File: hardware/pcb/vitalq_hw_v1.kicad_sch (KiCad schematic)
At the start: 2 parts

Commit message: Rebuild the hw_v1 board around the reduced part list.
Replace the stub hierarchy and import-grid PCB with an explicit
seven-sheet schematic and a 52 x 40 mm two-sided wearable placement.
AS7341 stays on a 1.8 V TPS7A2018, with one PCA9306 for its I2C bus.

Co-authored-by: Riyu-D1 <Riyu-D1@users.noreply.github.com>
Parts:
- removed PFLG1, PFLG2: PWR_FLAG, symbol power:PWR_FLAG
- added C1, C2: 4.7u, Capacitor_SMD:C_0402_1005Metric, symbol vitalq:C
- added C3, C4, C5, C6: 1u, Capacitor_SMD:C_0402_1005Metric, symbol vitalq:C
- added H1, H2: M2, MountingHole:MountingHole_2.2mm_M2, symbol vitalq:MountingHole
- added J1: USB-C, Connector_USB:USB_C_Receptacle_HRO_TYPE-C-31-M-12, symbol vitalq:USB_C_Receptacle_USB2.0_16P
- added J2: LiPo, Connector_JST:JST_PH_S2B-PH-SM4-TB_1x02-1MP_P2.00mm_Horizontal, symbol vitalq:Conn_01x02_Pin
- added R1, R2: 5.1k, Resistor_SMD:R_0402_1005Metric, symbol vitalq:R
- added R3: 10k, Resistor_SMD:R_0402_1005Metric, symbol vitalq:R
- added U2: MCP73831T-2ACI/OT, Package_TO_SOT_SMD:SOT-23-5, symbol vitalq:MCP73831-2-OT
- added U3: XC6206P332MR-G, Package_TO_SOT_SMD:SOT-23-3, symbol vitalq:XC6206PxxxMR
- added U4: TPS7A2018PDBVR, Package_TO_SOT_SMD:SOT-23-5, symbol vitalq:TPS7A2018PDBVR
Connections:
- net GND: now also C1.2, C2.2, C3.2, C4.2, C5.2, C6.2, J1.A1 (GND), J1.A12 (GND), J1.B1 (GND), J1.B12 (GND), J1.S1 (SHIELD), J2.2 (Pin_2), R1.2, R2.2, R3.2, U2.2 (V_{SS}), U3.1 (GND), U4.2 (GND)
- net VBUS: now also C1.1, J1.A4 (VBUS), J1.A9 (VBUS), J1.B4 (VBUS), J1.B9 (VBUS), U2.4 (V_{DD})
- new net +1V8: C6.1, U4.5 (OUT)
- new net +3V3: C4.1, C5.1, U3.2 (VO), U4.1 (IN), U4.3 (EN)
- new net CHG_PROG: R3.1, U2.5 (PROG)
- new net USB_CC1: J1.A5 (CC1), R1.1
- new net USB_CC2: J1.B5 (CC2), R2.1
- new net USB_DM: J1.A7 (D-), J1.B7 (D-)
- new net USB_DP: J1.A6 (D+), J1.B6 (D+)
- new net VBAT: C2.1, C3.1, J2.1 (Pin_1), U2.3 (V_{BAT}), U3.3 (VI)
- no-connect marks 0 -> 3
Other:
- removed sheet contact
- removed sheet i2c_sensors
- removed sheet mcu
- removed sheet power
- removed sheet spi_afes
- removed sheet usb
- added sheet AD5940 EDA (ad5940.kicad_sch)
- added sheet ADS1292R ECG (ads1292.kicad_sch)
- added sheet AFE4900 PPG (afe4900.kicad_sch)
- added sheet I2C and IMU (i2c.kicad_sch)
- added sheet MCU and FSR (mcu.kicad_sch)
- added sheet USB-UART (usb.kicad_sch)
- note added: "Decoupling"
- note added: "Load sits on VBAT. USB charges the cell and powers the UART. The board does not run from USB with the cell missing."
- note added: "Other sheets"
- note added: "Power and charging"
- note added: "R3 = 10k sets MCP73831 to 100 mA. STAT is open. No charge LED. H1 and H2 are M2 holes."
- note added: "Sheets below contain the parts. They are not empty stubs."
- note added: "TPS7A2018 (not 3.3 V): AS7341 VDD is 1.7-2.0 V. Every other IC runs at 3.3 V."
- note added: "U4 is fed from U3. EN is tied to IN. No separate 1.8 V XC6206."
- note added: "USB-C, LiPo charger, 3.3 V rail, 1.8 V rail"
- company: (none) -> VitalQ
- title: VitalQ hw_v1 research prototype — wiring only, not placed -> Power and charging

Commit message: Use official CAD and shrink the hw_v1 board to 37x30 mm.
Replace the hand-drawn AFE4900, AD5940, ADS1292R, AS7341, MLX90632,
TMP117, LSM6DSV80X, and MCP73831 symbols and footprints with the
SnapMagic and Ultra Librarian libraries. ADS1292R is now the QFN-32
ADS1292RIRSMT, and MLX90632SLD-DCB-100-SP moves SDA/SCL onto the
existing 1.8 V bus. Pin headers and mounting holes are flat solder
pads. The unrouted 4-layer placement keeps the antenna on the left
edge and the skin sensors together on the bottom.

Co-authored-by: Riyu-D1 <Riyu-D1@users.noreply.github.com>
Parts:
- removed H1, H2: M2, MountingHole:MountingHole_2.2mm_M2, symbol vitalq:MountingHole
- removed U2: MCP73831T-2ACI/OT, Package_TO_SOT_SMD:SOT-23-5, symbol vitalq:MCP73831-2-OT
- added U2: MCP73831T-2ACI/OT, snap:SOT95P280X145-5N, symbol vitalq:MCP73831T-2ACI_OT
- J2: value LiPo -> LiPo pads; footprint Connector_JST:JST_PH_S2B-PH-SM4-TB_1x02-1MP_P2.00mm_Horizontal -> vitalq:Pads_LiPo
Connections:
- net CHG_PROG: now also U2.5 (PROG)
- net GND: now also U2.2 (VSS)
- net VBAT: now also U2.3 (VBAT)
- net VBUS: now also U2.4 (VDD)
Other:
- note added: "J2 is two flat solder pads (BAT+ BAT-), not a header. No power switch."

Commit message: Pack the hw_v1 board to 36.2 x 28 mm and correct the 3D models.
The LSM6 body is a 3.0 x 2.5 x 0.83 mm box in KiCad VRML units, and the other vendor models are rotated so they stand on their lands. Skin sensors sit in one bottom cluster with the electrode pads around them, bypass parts are packed next to their ICs outside the antenna keep-out, and the schematic frames clear the title block.

Co-authored-by: Riyu-D1 <Riyu-D1@users.noreply.github.com>
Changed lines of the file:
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@@
 		(instances
 			(project "vitalq_hw_v1"
-				(path "/3a03f3a2-f664-49ab-a6e3-0e34faafa582"
+				(path "/6fcf6b13-4a8e-4f25-a8b9-d34cb547168d"
 					(reference "J1")
 					(unit 1)
@@
 		(instances
 			(project "vitalq_hw_v1"
-				(path "/3a03f3a2-f664-49ab-a6e3-0e34faafa582"
+				(path "/6fcf6b13-4a8e-4f25-a8b9-d34cb547168d"
 					(reference "#PWR001")
 					(unit 1)
@@
 		(instances
 			(project "vitalq_hw_v1"
-				(path "/3a03f3a2-f664-49ab-a6e3-0e34faafa582"
+				(path "/6fcf6b13-4a8e-4f25-a8b9-d34cb547168d"
 					(reference "#PWR002")
 					(unit 1)
@@
 		(instances
 			(project "vitalq_hw_v1"
-				(path "/3a03f3a2-f664-49ab-a6e3-0e34faafa582"
+				(path "/6fcf6b13-4a8e-4f25-a8b9-d34cb547168d"
 					(reference "R1")
 					(unit 1)
@@
 		(instances
 			(project "vitalq_hw_v1"
-				(path "/3a03f3a2-f664-49ab-a6e3-0e34faafa582"
+				(path "/6fcf6b13-4a8e-4f25-a8b9-d34cb547168d"
 					(reference "#PWR003")
 					(unit 1)
@@
 		(instances
 			(project "vitalq_hw_v1"
-				(path "/3a03f3a2-f664-49ab-a6e3-0e34faafa582"
+				(path "/6fcf6b13-4a8e-4f25-a8b9-d34cb547168d"
 					(reference "R2")
 					(unit 1)
@@
 		(instances
 			(project "vitalq_hw_v1"
-				(path "/3a03f3a2-f664-49ab-a6e3-0e34faafa582"
+				(path "/6fcf6b13-4a8e-4f25-a8b9-d34cb547168d"
 					(reference "#PWR004")
 					(unit 1)
@@
 		(instances
 			(project "vitalq_hw_v1"
-				(path "/3a03f3a2-f664-49ab-a6e3-0e34faafa582"
+				(path "/6fcf6b13-4a8e-4f25-a8b9-d34cb547168d"
 					(reference "U2")
 					(unit 1)
@@
 		(instances
 			(project "vitalq_hw_v1"
-				(path "/3a03f3a2-f664-49ab-a6e3-0e34faafa582"
+				(path "/6fcf6b13-4a8e-4f25-a8b9-d34cb547168d"
 					(reference "R3")
 					(unit 1)
@@
 		(instances
 			(project "vitalq_hw_v1"
-				(path "/3a03f3a2-f664-49ab-a6e3-0e34faafa582"
+				(path "/6fcf6b13-4a8e-4f25-a8b9-d34cb547168d"
 					(reference "#PWR005")
 					(unit 1)
@@
 		(instances
 			(project "vitalq_hw_v1"
-				(path "/3a03f3a2-f664-49ab-a6e3-0e34faafa582"
+				(path "/6fcf6b13-4a8e-4f25-a8b9-d34cb547168d"
 					(reference "U3")
 					(unit 1)
@@
 		(instances
 			(project "vitalq_hw_v1"
-				(path "/3a03f3a2-f664-49ab-a6e3-0e34faafa582"
+				(path "/6fcf6b13-4a8e-4f25-a8b9-d34cb547168d"
 					(reference "#PWR006")
 					(unit 1)
@@
 		(instances
 			(project "vitalq_hw_v1"
-				(path "/3a03f3a2-f664-49ab-a6e3-0e34faafa582"
+				(path "/6fcf6b13-4a8e-4f25-a8b9-d34cb547168d"
 					(reference "U4")
 					(unit 1)
@@
 		(instances
 			(project "vitalq_hw_v1"
-				(path "/3a03f3a2-f664-49ab-a6e3-0e34faafa582"
+				(path "/6fcf6b13-4a8e-4f25-a8b9-d34cb547168d"
 					(reference "#PWR007")
 					(unit 1)
@@
 		(instances
 			(project "vitalq_hw_v1"
-				(path "/3a03f3a2-f664-49ab-a6e3-0e34faafa582"
+				(path "/6fcf6b13-4a8e-4f25-a8b9-d34cb547168d"
 					(reference "J2")
 					(unit 1)
@@
 		(instances
 			(project "vitalq_hw_v1"
-				(path "/3a03f3a2-f664-49ab-a6e3-0e34faafa582"
+				(path "/6fcf6b13-4a8e-4f25-a8b9-d34cb547168d"
 					(reference "C1")
 					(unit 1)
@@
 		(instances
 			(project "vitalq_hw_v1"
-				(path "/3a03f3a2-f664-49ab-a6e3-0e34faafa582"
+				(path "/6fcf6b13-4a8e-4f25-a8b9-d34cb547168d"
 					(reference "#PWR008")
 					(unit 1)
@@
 		(instances
 			(project "vitalq_hw_v1"
-				(path "/3a03f3a2-f664-49ab-a6e3-0e34faafa582"
+				(path "/6fcf6b13-4a8e-4f25-a8b9-d34cb547168d"
 					(reference "#PWR009")
 					(unit 1)
@@
 		(instances
 			(project "vitalq_hw_v1"
-				(path "/3a03f3a2-f664-49ab-a6e3-0e34faafa582"
+				(path "/6fcf6b13-4a8e-4f25-a8b9-d34cb547168d"
 					(reference "C2")
 					(unit 1)
@@
 		(instances
 			(project "vitalq_hw_v1"
-				(path "/3a03f3a2-f664-49ab-a6e3-0e34faafa582"
+				(path "/6fcf6b13-4a8e-4f25-a8b9-d34cb547168d"
 					(reference "#PWR010")
 					(unit 1)
@@
 		(instances
 			(project "vitalq_hw_v1"
-				(path "/3a03f3a2-f664-49ab-a6e3-0e34faafa582"
+				(path "/6fcf6b13-4a8e-4f25-a8b9-d34cb547168d"
 					(reference "C3")
 					(unit 1)
@@
 		(instances
 			(project "vitalq_hw_v1"
-				(path "/3a03f3a2-f664-49ab-a6e3-0e34faafa582"
+				(path "/6fcf6b13-4a8e-4f25-a8b9-d34cb547168d"
 					(reference "#PWR011")
 					(unit 1)
@@
 		(instances
 			(project "vitalq_hw_v1"
-				(path "/3a03f3a2-f664-49ab-a6e3-0e34faafa582"
+				(path "/6fcf6b13-4a8e-4f25-a8b9-d34cb547168d"
 					(reference "C4")
 					(unit 1)
@@
 		(instances
 			(project "vitalq_hw_v1"
-				(path "/3a03f3a2-f664-49ab-a6e3-0e34faafa582"
+				(path "/6fcf6b13-4a8e-4f25-a8b9-d34cb547168d"
 					(reference "#PWR012")
 					(unit 1)
@@
 		(instances
 			(project "vitalq_hw_v1"
-				(path "/3a03f3a2-f664-49ab-a6e3-0e34faafa582"
+				(path "/6fcf6b13-4a8e-4f25-a8b9-d34cb547168d"
 					(reference "#PWR013")
 					(unit 1)
@@
 		(instances
 			(project "vitalq_hw_v1"
-				(path "/3a03f3a2-f664-49ab-a6e3-0e34faafa582"
+				(path "/6fcf6b13-4a8e-4f25-a8b9-d34cb547168d"
 					(reference "C5")
 					(unit 1)
@@
 		(instances
 			(project "vitalq_hw_v1"
-				(path "/3a03f3a2-f664-49ab-a6e3-0e34faafa582"
+				(path "/6fcf6b13-4a8e-4f25-a8b9-d34cb547168d"
 					(reference "#PWR014")
 					(unit 1)
@@
 		(instances
 			(project "vitalq_hw_v1"
-				(path "/3a03f3a2-f664-49ab-a6e3-0e34faafa582"
+				(path "/6fcf6b13-4a8e-4f25-a8b9-d34cb547168d"
 					(reference "#PWR015")
 					(unit 1)
@@
 		(instances
 			(project "vitalq_hw_v1"
-				(path "/3a03f3a2-f664-49ab-a6e3-0e34faafa582"
+				(path "/6fcf6b13-4a8e-4f25-a8b9-d34cb547168d"
 					(reference "C6")
 					(unit 1)
@@
 		(instances
 			(project "vitalq_hw_v1"
-				(path "/3a03f3a2-f664-49ab-a6e3-0e34faafa582"
+				(path "/6fcf6b13-4a8e-4f25-a8b9-d34cb547168d"
 					(reference "#PWR016")
 					(unit 1)
@@
 		(instances
 			(project "vitalq_hw_v1"
-				(path "/3a03f3a2-f664-49ab-a6e3-0e34faafa582"
+				(path "/6fcf6b13-4a8e-4f25-a8b9-d34cb547168d"
 					(reference "#PWR017")
 					(unit 1)
@@
 		(instances
 			(project "vitalq_hw_v1"
-				(path "/3a03f3a2-f664-49ab-a6e3-0e34faafa582"
+				(path "/6fcf6b13-4a8e-4f25-a8b9-d34cb547168d"
 					(reference "#PWR018")
 					(unit 1)
@@
 		(instances
 			(project "vitalq_hw_v1"
-				(path "/3a03f3a2-f664-49ab-a6e3-0e34faafa582"
+				(path "/6fcf6b13-4a8e-4f25-a8b9-d34cb547168d"
 					(reference "#FLG019")
 					(unit 1)
@@
 		(instances
 			(project "vitalq_hw_v1"
-				(path "/3a03f3a2-f664-49ab-a6e3-0e34faafa582"
+				(path "/6fcf6b13-4a8e-4f25-a8b9-d34cb547168d"
 					(reference "#PWR020")
 					(unit 1)
@@
 		(instances
 			(project "vitalq_hw_v1"
-				(path "/3a03f3a2-f664-49ab-a6e3-0e34faafa582"
+				(path "/6fcf6b13-4a8e-4f25-a8b9-d34cb547168d"
 					(reference "#FLG021")
 					(unit 1)
@@
 	)
 	(rectangle
-		(start 12.0 20.0)
-		(end 408.0 200.0)
+		(start 12.0 40.0)
+		(end 406.0 200.0)
 		(stroke (width 0.4) (type dash))
 		(fill (type none))
@@
 		(instances
 			(project "vitalq_hw_v1"
-				(path "/3a03f3a2-f664-49ab-a6e3-0e34faafa582"
+				(path "/6fcf6b13-4a8e-4f25-a8b9-d34cb547168d"
 					(page "2")
 				)
@@
 		(instances
 			(project "vitalq_hw_v1"
-				(path "/3a03f3a2-f664-49ab-a6e3-0e34faafa582"
+				(path "/6fcf6b13-4a8e-4f25-a8b9-d34cb547168d"
 					(page "3")
 				)
@@
 		(instances
 			(project "vitalq_hw_v1"
-				(path "/3a03f3a2-f664-49ab-a6e3-0e34faafa582"
+				(path "/6fcf6b13-4a8e-4f25-a8b9-d34cb547168d"
 					(page "4")
 				)
@@
 		(instances
 			(project "vitalq_hw_v1"
-				(path "/3a03f3a2-f664-49ab-a6e3-0e34faafa582"
+				(path "/6fcf6b13-4a8e-4f25-a8b9-d34cb547168d"
 					(page "5")
 				)
@@
 		(instances
 			(project "vitalq_hw_v1"
-				(path "/3a03f3a2-f664-49ab-a6e3-0e34faafa582"
+				(path "/6fcf6b13-4a8e-4f25-a8b9-d34cb547168d"
 					(page "6")
 				)
@@
 		(instances
 			(project "vitalq_hw_v1"
-				(path "/3a03f3a2-f664-49ab-a6e3-0e34faafa582"
+				(path "/6fcf6b13-4a8e-4f25-a8b9-d34cb547168d"
 					(page "7")
 				)

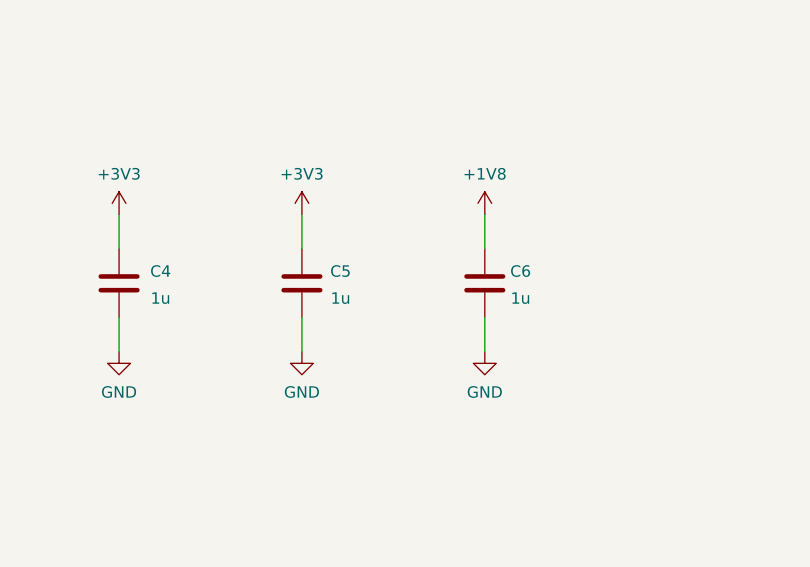
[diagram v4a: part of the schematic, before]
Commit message: Seat the QFN models and drop passives the datasheets do not require.
The ADS1292R STEP is already Z-up, so the extra X rotation stood the
4x4x1 mm body on edge. Remove TP1, TP2, C5, C12, C17, C31 and R4, add
the 1 uF AVDD bulk capacitor, and shorten the outline to 36.2 x 27.8 mm.

Co-authored-by: Riyu-D1 <Riyu-D1@users.noreply.github.com>
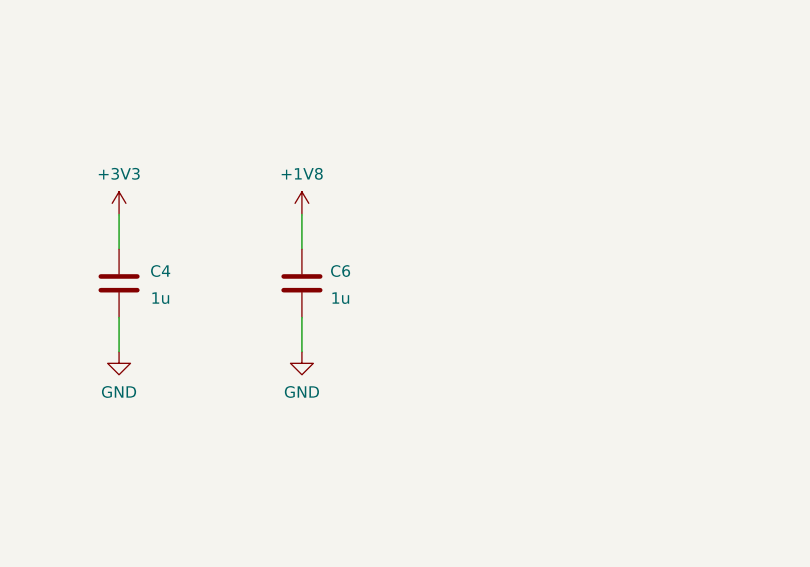
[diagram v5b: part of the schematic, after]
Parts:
- removed C5: 1u, Capacitor_SMD:C_0402_1005Metric, symbol vitalq:C

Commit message: Add the chest-board sensors and replace the 3.3 V LDO with a TPS63802.
The unrouted 40 x 34 mm board keeps every previous part except the off-board PPG pads, which the SFH 7072 replaces. Respiration, a second ECG lead, electrode protection, EDA, fuel gauge, flash, and the I/O expander are in the schematic.

Co-authored-by: Riyu-D1 <Riyu-D1@users.noreply.github.com>
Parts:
- removed U3: XC6206P332MR-G, Package_TO_SOT_SMD:SOT-23-3, symbol vitalq:XC6206PxxxMR
- added C44: 10u, Capacitor_SMD:C_0603_1608Metric, symbol vitalq:C
- added C45: 22u, Capacitor_SMD:C_0603_1608Metric, symbol vitalq:C
- added C58: 100n, Capacitor_SMD:C_0402_1005Metric, symbol vitalq:C
- added L1: 0.47u, vitalq:L_DFE201612E, symbol vitalq:L
- added R23: 560k, Resistor_SMD:R_0402_1005Metric, symbol vitalq:R
- added R24, R50: 100k, Resistor_SMD:R_0402_1005Metric, symbol vitalq:R
- added R49: 10k, Resistor_SMD:R_0402_1005Metric, symbol vitalq:R
- added R51: 200k, Resistor_SMD:R_0402_1005Metric, symbol vitalq:R
- added U17: MAX17048G+T10, vitalq:MAX17048_WLP, symbol vitalq:MAX17048
- added U3: TPS63802DLAR, Package_SON:WSON-10-1EP_2x3mm_P0.5mm_EP0.84x2.4mm, symbol vitalq:TPS63802
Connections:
- net +3V3: now also C45.1, R23.1, R49.1, U3.6 (VOUT)
- net GND: now also C44.2, C45.2, C58.2, R24.2, R51.2, U17.A1 (CTG), U17.A4 (GND), U17.B3 (QSTRT), U3.11 (EP), U3.2 (MODE), U3.3 (AGND), U3.8 (GND)
- net VBAT: now also C44.1, C58.1, U17.A2 (CELL), U17.A3 (VDD), U3.1 (EN), U3.10 (VIN)
- net VBUS: now also R50.1
- net CHG_STAT: now reaches U2.1 (STAT)
- net CHG_STAT: now also R49.2
- new net FB_3V3: R23.2, R24.1, U3.4 (FB)
- new net I2C_SCL: U17.B2 (SCL)
- new net I2C_SDA: U17.B1 (SDA)
- new net SW_L1: L1.1, U3.9 (L1)
- new net SW_L2: L1.2, U3.7 (L2)
- new net VBUS_DET: R50.2, R51.1
- no-connect marks 3 -> 4
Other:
- note added: "Load sits on VBAT. U17 is the MAX17048 (0x36). R49 pulls STAT up. R50/R51 divide VBUS to about 3.3 V."
- note added: "U3 is a TPS63802 buck-boost. R23/R24 set 3.30 V. C44 and C45 are the datasheet 0603 ceramics. C3 and C4 stay."
- note added: "U4 is the 1.8 V LDO, fed from U3, EN tied to IN. AS7341 VDD is 1.7-2.0 V. Other ICs are 3.3 V."
- note removed: "Load sits on VBAT. USB charges the cell and powers the UART. The board does not run from USB with the cell missing."
- note removed: "R3 = 10k sets MCP73831 to 100 mA. STAT is open. No charge LED. H1 and H2 are M2 holes."
- note removed: "TPS7A2018 (not 3.3 V): AS7341 VDD is 1.7-2.0 V. Every other IC runs at 3.3 V."
- note removed: "U4 is fed from U3. EN is tied to IN. No separate 1.8 V XC6206."

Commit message: Add defibrillator clamps and a charge-temperature cut-off.
Series electrode resistors are now DPCR2512 51k pulse parts, with an S30-A90X gas discharge tube on each patient pad ahead of the existing TPD1E10B06. The MCP73831 stays; a PicoStar FET floats PROG until firmware enables charge, and a 3-pin cell pad feeds a 10k NTC into GPIO39.

Co-authored-by: Riyu-D1 <Riyu-D1@users.noreply.github.com>
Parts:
- removed J2: LiPo pads, vitalq:Pads_LiPo, symbol vitalq:Conn_01x02_Pin
- added J2: LiPo pads, vitalq:Pads_LiPo, symbol vitalq:Conn_01x03_Pin
- added Q2: CSD13380F3, Package_DFN_QFN:Texas_PicoStar_DFN-3_0.69x0.60mm, symbol vitalq:CSD13380F3
- added R59: 100k, Resistor_SMD:R_0402_1005Metric, symbol vitalq:R
- added R60, R61: 10k, Resistor_SMD:R_0402_1005Metric, symbol vitalq:R
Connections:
- net +3V3: now also R60.1
- net GND: now also J2.2 (Pin_2), Q2.2 (S), R59.2, R61.2; no longer R3.2
- net VBAT: now also J2.1 (Pin_1)
- new net CHG_EN: Q2.1 (G), R59.1
- new net NTC_ADC: J2.3 (Pin_3), R60.2, R61.1
- new net PROG_RTN: Q2.3 (D), R3.2
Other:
- note added: "Charge stays off at power-up: the expander port is Hi-Z and R59 holds the gate low."
- note added: "J2 is three flat pads (BAT+ BAT- NTC), not a header. No power switch."
- note added: "R61 is the on-board 10k NTC, DNP. Fit it or the cell NTC, not both. Q2 floats PROG until CHG_EN is high."
- note removed: "J2 is two flat solder pads (BAT+ BAT-), not a header. No power switch."
